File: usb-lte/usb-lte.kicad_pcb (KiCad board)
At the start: 4 copper layers, 26 x 45 mm, 90 parts, among them J1 Sim slot, J2 Conn_Coaxial, J3 Conn_Coaxial, J4 Conn_Coaxial, P1 USB_C_Plug_USB2.0, Q1 MBT3904DW1, Q2 MBT3904DW1, Q3 MBT3904DW1, U1 TPS62A02APDDC, U2 EG95

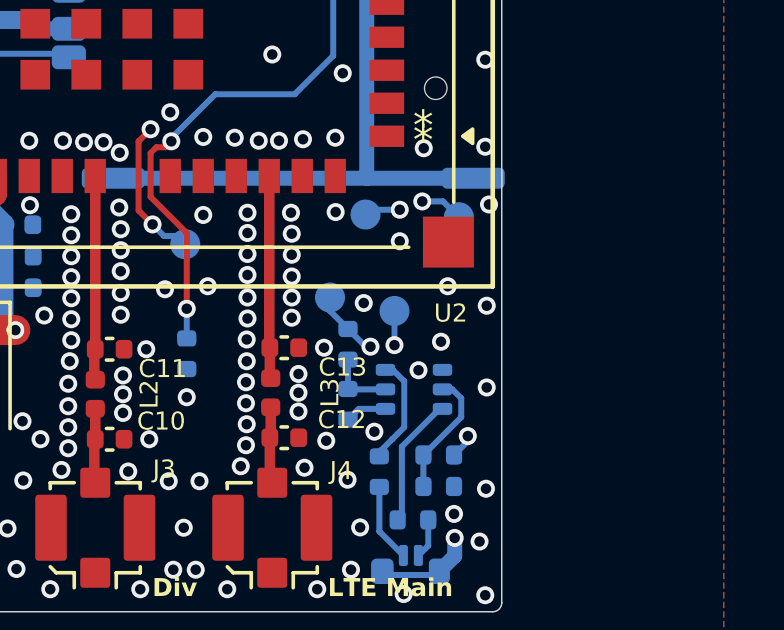
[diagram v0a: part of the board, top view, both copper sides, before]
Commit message: Fix SMPS chip variant number
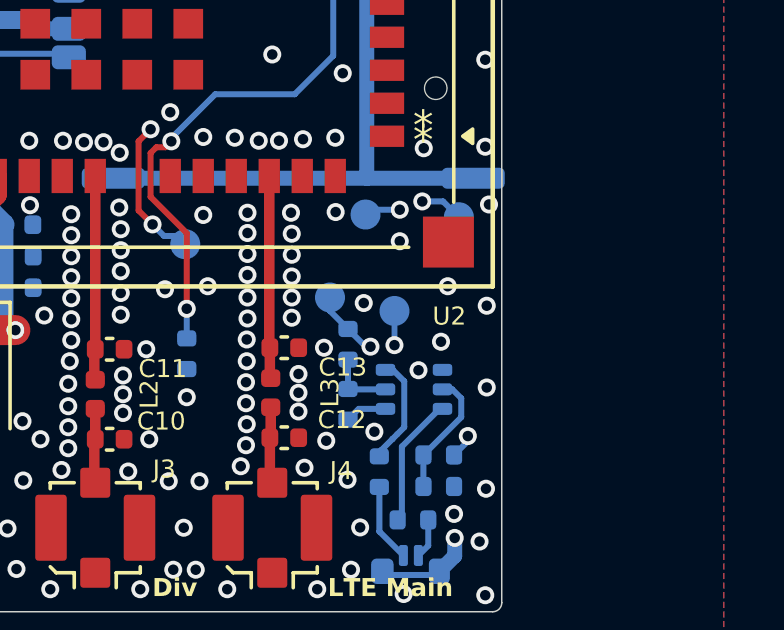
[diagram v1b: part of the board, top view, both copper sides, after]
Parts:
- U1: value TPS62A02APDDC -> TPS62A02ADRL
